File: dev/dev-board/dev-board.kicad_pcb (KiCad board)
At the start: 4 copper layers, 90 x 70 mm, 123 parts, among them J5 Conn_02x10_Odd_Even, P1 HDR-IDC-2.54-2X5P, Q1 BSS138, Q2 BSS138, Q3 BSS138, Q4 BSS138, SW1 TS342A2P, SW2 TS342A2P, SW3 TS342A2P, SW4 TS342A2P, SW5 TS342A2P, SW6 TS342A2P, SW7 TS342A2P, SW8 TS342A2P, U1 ESP32-WROVER-IE(16MB), U10 TPS2065CDBV, U11 PESD5V0U2BT, U12 PESD5V0S1BA_C5261083, U13 PCM5102APWR, U14 CH340C, U16 PESD5V0U2BT, U2 ESP32-S3-WROOM-1(N16R8), U3 CH340C, U4 TPS2065CDBV, U5 AP7361C-33E, U6 PESD5V0U2BT, U7 PESD5V0S1BA_C5261083, U8 ZX-HY2.0-4PWZ, U9 ZX-HY2.0-4PWZ

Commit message: wiring donw. checking DRC
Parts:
- moved C6 13.6 mm to (90.0, 200.8), turned to -90 degrees
- moved R10 12.2 mm to (102.0, 208.2)
- moved R3 11.5 mm to (89.8, 197.0), turned to -90 degrees
- moved TP1 11.3 mm to (100.0, 200.5)
- moved TP2 10.3 mm to (73.2, 203.5)
- moved TP4 10.1 mm to (76.8, 203.5)
- moved C12 8.38 mm to (48.5, 206.0)
- moved R37 5.27 mm to (83.0, 202.5), turned to -90 degrees
- moved Q2 3.76 mm to (56.0, 203.5)
- moved R5 3.51 mm to (89.2, 212.5)
- moved R9 3.48 mm to (89.2, 210.5)
- moved R12 3.04 mm to (48.5, 213.5)
- moved R7 2.30 mm to (104.8, 197.0), turned to 90 degrees
- moved C4 2.06 mm to (89.8, 193.5), turned to 90 degrees
- moved D3 2.05 mm to (61.2, 246.5)
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- renumbered TX1 to TP1, TX2 to TP2, RX1 to TP3, RX2 to TP4
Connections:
- J5 pad 10: /WR-IO35 -> /WR-IO36
- J5 pad 4: /WR-IO36 -> /WR-IO35
- J5 pad 6: /WR-IO39 -> /WR-IO34
- J5 pad 8: /WR-IO34 -> /WR-IO39
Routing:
- net GND: track 5.82 -> 151.0 mm, vias 3 -> 80
- net /S3-ButtonUp: track 0.00 -> 98.1 mm, vias 0 -> 4
- net /S3-IO0: track 0.00 -> 97.4 mm, vias 0 -> 4
- net /S3-ButtonCancel: track 0.00 -> 97.3 mm, vias 0 -> 4
- net /S3-ButtonDown: track 0.00 -> 93.2 mm, vias 0 -> 4
- net /S3-ButtonEnter: track 0.00 -> 84.2 mm, vias 0 -> 5
- net /S3-USB-PWSW: track 12.5 -> 89.1 mm, vias 0 -> 2
- net /S3-EN: track 0.00 -> 71.7 mm, vias 0 -> 6
- net /S3-I2C1-SDA: track 0.00 -> 67.9 mm
- net /WR-IO15: track 0.00 -> 64.6 mm, vias 0 -> 4
- net /S3-I2C1-SCL: track 0.00 -> 64.2 mm
- net /S3-ResetSub: track 0.00 -> 63.4 mm, vias 0 -> 4
- net /WR-IO12: track 0.00 -> 59.0 mm, vias 0 -> 1
- net VSYS: track 37.1 -> 95.8 mm, vias 13 -> 14
- net /WR-IO4: track 0.00 -> 58.1 mm, vias 0 -> 1
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- added copper zone on F.Cu, net GND

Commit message: checking before release
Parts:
- added G***: LOGO, LogoLibrary:logo_sym.kicad2_mod, F.Cu at (110.0, 248.0)
- moved C22 1.75 mm to (45.5, 241.5)
- moved C23 1.75 mm to (45.5, 239.8)
- renumbered SW6 to Cancel, SW8 to DOWN, SW7 to Enter, TP3 to RX1, TP4 to RX2, SW3 to S3-EN, SW1 to S3-IO0, TP1 to TX1, TP2 to TX2, SW5 to UP, SW4 to WR-EN, SW2 to WR-IO0
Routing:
- net GND: track 151.0 -> 219.7 mm, vias 80 -> 315
- net /S3-ButtonEnter: track 84.2 -> 78.9 mm
- net /S3-MTMS: track 34.8 -> 37.1 mm
- net +3V3: track 78.7 -> 80.2 mm
- net /S3-IO0: track 97.4 -> 96.7 mm
- net /WR-IO14: track 49.7 -> 50.2 mm
- net /WR-IO15: track 64.6 -> 65.1 mm
- added copper zone on B.Cu, net GND
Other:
- board text added: "Narya v3 dev R2"

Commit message: r2 candidate
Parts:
- turned C30 to 180 degrees
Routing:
- net GND: track 219.7 -> 234.5 mm, vias 315 -> 309
- net Net-(LDO1-VOUT): track 29.5 -> 22.2 mm
- net Net-(U13-CPGND): track 10.5 -> 6.14 mm
- net /S3-EN: track 71.7 -> 74.9 mm
- net /S3-ResetSub: track 63.4 -> 65.9 mm
- net /S3-ButtonDown: track 93.2 -> 95.3 mm
- net +3V3: track 80.2 -> 82.3 mm, vias 30 -> 29
- net /S3-ButtonEnter: track 78.9 -> 80.9 mm
- net Net-(U13-XSMT): track 6.15 -> 7.69 mm

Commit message: r2 candidate (fix CH340 V3-VCC)
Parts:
- renumbered S3-IO0 to SW1, WR-IO0 to SW2, S3-EN to SW3, WR-EN to SW4, UP to SW5, Cancel to SW6, Enter to SW7, DOWN to SW8
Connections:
- C4 pad 2: Net-(U3-V3) -> +3V3
- C5 pad 2: Net-(U14-V3) -> +3V3
- U14 pad 4: Net-(U14-V3) -> +3V3
- U3 pad 4: Net-(U3-V3) -> +3V3
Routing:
- net +3V3: track 82.3 -> 106.9 mm, vias 29 -> 31
- net Net-(U3-V3): track 11.9 -> 0.00 mm
- net Net-(U14-V3): track 10.4 -> 0.00 mm
- net GND: vias 309 -> 307

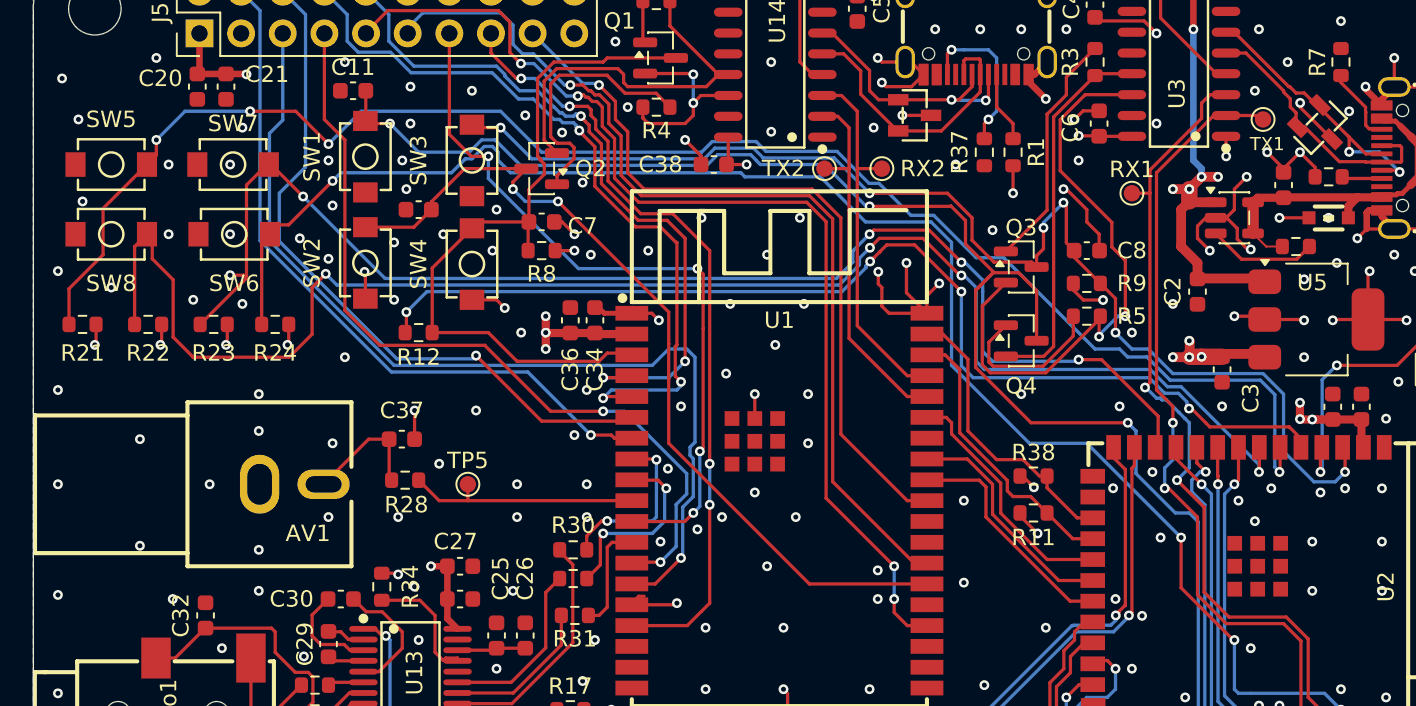
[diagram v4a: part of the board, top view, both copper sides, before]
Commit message: r2 candidate (fix silk, add via around ESP32 GND pad)
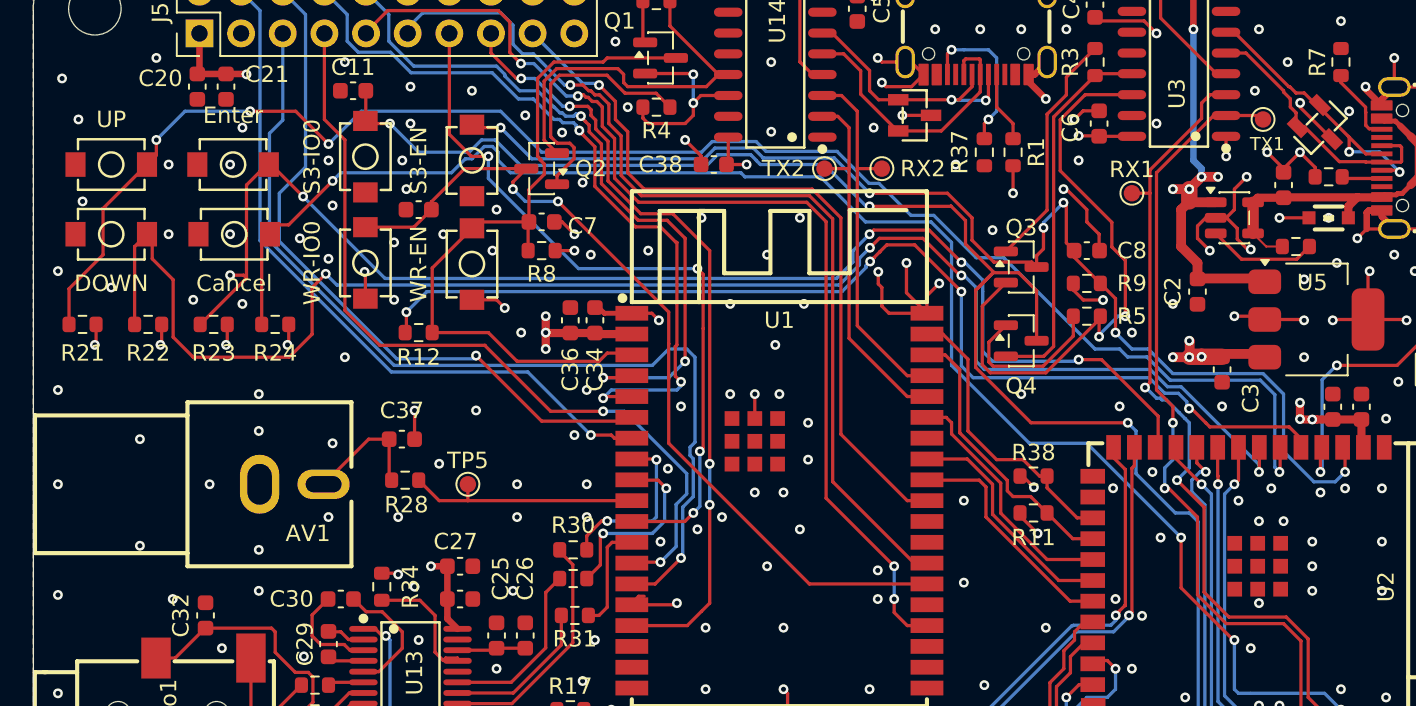
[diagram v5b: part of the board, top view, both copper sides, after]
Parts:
- renumbered SW6 to Cancel, SW8 to DOWN, SW7 to Enter, SW3 to S3-EN, SW1 to S3-IO0, SW5 to UP, SW4 to WR-EN, SW2 to WR-IO0
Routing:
- net GND: track 234.5 -> 239.7 mm, vias 307 -> 312
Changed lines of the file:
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@@
 		(layer "F.Cu")
 		(at 51.75 203 90)
-		(property "Reference" "SW3"
+		(property "Reference" "S3-EN"
 			(at 0 -3.25 90)
 			(layer "F.SilkS")
@@
 		(layer "F.Cu")
 		(at 45.25 202.77 90)
-		(property "Reference" "SW1"
+		(property "Reference" "S3-IO0"
 			(at 0 -3.25 90)
 			(layer "F.SilkS")
@@
 				(font
 					(size 1 1)
-					(thickness 0.15)
+					(thickness 0.125)
 				)
 			)
@@
 		(layer "F.Cu")
 		(at 45.25 209.25 90)
-		(property "Reference" "SW2"
+		(property "Reference" "WR-IO0"
 			(at 0 -3.25 90)
 			(layer "F.SilkS")
@@
 		(layer "F.Cu")
 		(at 37.18 203.25)
-		(property "Reference" "SW7"
-			(at 0 -2.5 0)
+		(property "Reference" "Enter"
+			(at 0 -3 0)
 			(layer "F.SilkS")
 			(effects
@@
 		(layer "F.Cu")
 		(at 37.25 207.5)
-		(property "Reference" "SW6"
+		(property "Reference" "Cancel"
 			(at 0 3 0)
 			(layer "F.SilkS")
@@
 		(layer "F.Cu")
 		(at 29.75 203.25)
-		(property "Reference" "SW5"
+		(property "Reference" "UP"
 			(at 0 -2.75 0)
 			(layer "F.SilkS")
@@
 		(layer "F.Cu")
 		(at 29.75 207.5)
-		(property "Reference" "SW8"
+		(property "Reference" "DOWN"
 			(at 0 3 0)
 			(layer "F.SilkS")
@@
 		(layer "F.Cu")
 		(at 51.75 209.32 90)
-		(property "Reference" "SW4"
+		(property "Reference" "WR-EN"
 			(at 0 -3.25 90)
 			(layer "F.SilkS")
@@
 	)
 	(via
+		(at 99.75 230)
+		(size 0.6)
+		(drill 0.3)
+		(layers "F.Cu" "B.Cu")
+		(free yes)
+		(net 3)
+	)
+	(via
 		(at 91 239.5)
 		(size 0.6)
@@
 	)
 	(via
-		(at 99.5 225)
+		(at 99.75 225)
 		(size 0.6)
 		(drill 0.3)
@@
 	)
 	(via
+		(at 101.25 225)
+		(size 0.6)
+		(drill 0.3)
+		(layers "F.Cu" "B.Cu")
+		(free yes)
+		(net 3)
+	)
+	(via
 		(at 60.5 195.75)
 		(size 0.6)
@@
 	)
 	(via
-		(at 72.25 220.25)
+		(at 72.25 221.25)
 		(size 0.6)
 		(drill 0.3)
@@
 	)
 	(via
-		(at 72.25 217.25)
+		(at 72.25 219)
 		(size 0.6)
 		(drill 0.3)
@@
 	)
 	(via
+		(at 103 227.75)
+		(size 0.6)
+		(drill 0.3)
+		(layers "F.Cu" "B.Cu")
+		(free yes)
+		(net 3)
+	)
+	(via
 		(at 81.5 254.75)
 		(size 0.6)
@@
 	)
 	(via
+		(at 70.75 223.25)
+		(size 0.6)
+		(drill 0.3)
+		(layers "F.Cu" "B.Cu")
+		(free yes)
+		(net 3)
+	)
+	(via
 		(at 107.5 218.75)
 		(size 0.6)
@@
 	)
 	(via
-		(at 71.5 224.75)
+		(at 71.75 225.5)
 		(size 0.6)
 		(drill 0.3)
@@
 	)
 	(via
+		(at 70.5 217.25)
+		(size 0.6)
+		(drill 0.3)
+		(layers "F.Cu" "B.Cu")
+		(free yes)
+		(net 3)
+	)
+	(via
 		(at 42.25 242)
 		(size 0.6)
@@
 	)
 	(via
-		(at 67.25 216)
+		(at 67.5 217.25)
 		(size 0.6)
 		(drill 0.3)
@@
 	)
 	(segment
-		(start 99.5 225)
-		(end 93.75 225)
+		(start 69 211.25)
+		(end 66.25 208.5)
 		(width 0.2)
 		(layer "In1.Cu")
@@
 	)
 	(segment
-		(start 69 217.25)
-		(end 69 212.09853)
-		(width 0.2)
-		(layer "In1.Cu")
-		(net 3)
-	)
-	(segment
 		(start 92.75 230.642209)
 		(end 92.617314 230.774895)
@@
 	)
 	(segment
+		(start 93.25 222)
+		(end 91.844321 222)
+		(width 0.2)
+		(layer "In1.Cu")
+		(net 3)
+	)
+	(segment
 		(start 92.875 225.875)
 		(end 92.75 226)
@@
 	)
 	(segment
-		(start 69 212.09853)
-		(end 65.450735 208.549265)
+		(start 55.5 249)
+		(end 57.5 249)
 		(width 0.2)
 		(layer "In1.Cu")
@@
 	)
 	(segment
-		(start 55.5 249)
-		(end 57.5 249)
+		(start 98.475737 240.324266)
+		(end 99.002471 240.851)
 		(width 0.2)
 		(layer "In1.Cu")
@@
 	)
 	(segment
-		(start 98.475737 240.324266)
-		(end 99.002471 240.851)
+		(start 66 208.5)
+		(end 65.75 208.25)
 		(width 0.2)
 		(layer "In1.Cu")
@@
 	)
 	(segment
-		(start 93.75 225)
-		(end 92.875 225.875)
-		(width 0.2)
-		(layer "In1.Cu")
-		(net 3)
-	)
-	(segment
 		(start 69 217.25)
 		(end 65.25 217.25)
@@
 	)
 	(segment
+		(start 91.844321 222)
+		(end 90.852216 222.992105)
+		(width 0.2)
+		(layer "In1.Cu")
+		(net 3)
+	)
+	(segment
+		(start 93.75 225)
+		(end 92.875 225.875)
+		(width 0.2)
+		(layer "In1.Cu")
+		(net 3)
+	)
+	(segment
 		(start 57.5 249)
 		(end 58.5 250)
@@
 	)
 	(segment
+		(start 66.25 208.5)
+		(end 66 208.5)
+		(width 0.2)
+		(layer "In1.Cu")
+		(net 3)
+	)
+	(segment
+		(start 69 217.25)
+		(end 69 211.25)
+		(width 0.2)
+		(layer "In1.Cu")
+		(net 3)
+	)
+	(segment
 		(start 58 217.75)
 		(end 58.75 217)
@@
 	)
 	(segment
+		(start 65.75 208.25)
+		(end 65.75 206.5)
+		(width 0.2)
+		(layer "In1.Cu")
+		(net 3)
+	)
+	(segment
 		(start 64.201 222.29953)
 		(end 63.700735 221.799265)
@@
 	)
 	(segment
+		(start 99.75 225)
+		(end 93.75 225)
+		(width 0.2)
+		(layer "In1.Cu")
+		(net 3)
+	)
+	(segment
 		(start 102.25 240)
 		(end 102.75 240)
@@
 		(polygon
 			(pts
-				(xy 34.25 250) (xy 58 250) (xy 64.5 241) (xy 73.75 241) (xy 73.75 220) (xy 94.75 207.75) (xy 98 205.75)
-				(xy 98 203.75) (xy 97 203) (xy 59.75 219.25) (xy 59.75 234.25) (xy 49.75 240.75) (xy 34.25 240.75)
+				(xy 34.25 250) (xy 58 250) (xy 64.5 241) (xy 74.5 241) (xy 79.25 217.5) (xy 95.75 206.5) (xy 98 205.75)
+				(xy 98 203.75) (xy 97 203) (xy 59.75 219.25) (xy 59.75 234.25) (xy 49.75 240.75) (xy 35 240.75)
 			)
 		)

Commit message: update for v3r3
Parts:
- removed RX1, RX2, TX1, TX2: TestPoint, TestPoint:TestPoint_Pad_D1.0mm
- added C17: 0.1uF, Capacitor_SMD:C_0603_1608Metric, F.Cu at (8.27, 54.0)
- added C39: 0.1uF, Capacitor_SMD:C_0603_1608Metric, F.Cu at (8.27, 55.5)
- added ERR1: LED RED, LED_SMD:LED_0805_2012Metric, F.Cu at (83.5, 60.0)
- added J1: Conn_01x03_Pin, Connector_PinHeader_2.54mm:PinHeader_1x03_P2.54mm_Vertical, F.Cu at (21.5, 58.7)
- added J2: Conn_01x02_Socket, Connector_PinSocket_2.54mm:PinSocket_1x02_P2.54mm_Vertical, F.Cu at (4.77, 52.3)
- added R39: 0, Resistor_SMD:R_0603_1608Metric, F.Cu at (80.3, 53.5)
- added R40: 0, Resistor_SMD:R_0603_1608Metric, F.Cu at (5.02, 55.8)
- added R41: 0, Resistor_SMD:R_0603_1608Metric, F.Cu at (11.3, 54.5)
- added R42: 0, Resistor_SMD:R_0603_1608Metric, F.Cu at (23.5, 23.5)
- added SW9: GT-TC018A-H0375-L1, easyeda2kicad:SW-SMD_L4.7-W3.5-P3.35-EH, F.Cu at (87.5, 57.8)
- added TP1: TestPoint, TestPoint:TestPoint_Pad_D1.0mm, F.Cu at (2.77, 58.8)
- added U15: RX8900CE_UB0, easyeda2kicad:SMD-10_L3.2-W2.5-BL_EPSON_RX8900CE, F.Cu at (6.77, 58.5)
- R12: value 100 -> 10K
- R15: value 10K -> 0
- R16: value 10K -> 2K
- moved G*** 209.9 mm to (59.5, 44.2)
- moved R16 197.4 mm to (83.5, 53.0), turned to 0 degrees
- moved C31 195.1 mm to (14.8, 48.5)
- moved Audio1 194.1 mm to (9.02, 44.2)
- moved C32 194.1 mm to (10.5, 38.2)
- moved REF4 193.6 mm to (84.8, 64.5)
- moved AV1 193.4 mm to (15.8, 31.0)
- moved REF2 193.2 mm to (5.52, 64.5)
- moved C1 191.6 mm to (76.3, 14.5)
- moved C10 191.6 mm to (12.3, 59.2)
- moved C11 191.6 mm to (19.5, 8.75)
- moved C12 191.6 mm to (23.5, 16.0)
- moved C13 191.6 mm to (26.5, 59.2)
- moved C14 191.6 mm to (34.0, 51.2)
- moved C15 191.6 mm to (43.8, 49.0)
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- renumbered Cancel to CANCEL, P1 to JTAG, REF** to REF1, REF** to REF2, REF** to REF3, REF** to REF4, D1 to STAT1
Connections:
- C13 pad 2: VSYS -> Net-(J1-Pin_2)
- R12 pad 1: /S3-ResetSub -> +3V3
- R12 pad 2: /WR-EN -> Net-(U15-~{INT})
- R15 pad 1: /S3-I2C2-SDA -> Net-(U15-~{INT})
- R15 pad 2: +3V3 -> /S3-MTDO
- R16 pad 1: /S3-I2C2-SCL -> Net-(D4-A)
- R16 pad 2: +3V3 -> Net-(R16-Pad2)
- U9 pad 2: VSYS -> Net-(J1-Pin_2)
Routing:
- net Net-(U15-~{INT}): track 0.00 -> 53.8 mm, vias 0 -> 2
- net /S3-EN: track 74.9 -> 104.8 mm, vias 6 -> 7
- net /S3-MTCK: track 24.7 -> 50.4 mm, vias 2 -> 3
- net /S3-I2C1-SCL: track 64.2 -> 84.8 mm
- net /S3-I2C1-SDA: track 67.9 -> 84.8 mm, vias 0 -> 1
- net /S3-StatLED1: track 15.2 -> 26.8 mm, vias 2 -> 0
- net /WR-NTSC: track 14.5 -> 5.13 mm
- net Net-(J1-Pin_2): track 0.00 -> 9.08 mm
- net Net-(D4-A): track 0.00 -> 8.48 mm
- net Net-(J2-Pin_1): track 0.00 -> 8.06 mm
- net Net-(AV1-Pad2): track 7.70 -> 15.1 mm
- net Net-(R16-Pad2): track 0.00 -> 5.50 mm, vias 0 -> 2
- net Net-(D1-A): track 2.30 -> 7.04 mm
- net /S3-I2C2-SDA: track 56.8 -> 52.4 mm, vias 2 -> 1
- net Net-(U15-FOUT): track 0.00 -> 4.15 mm, vias 0 -> 2
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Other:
- board text added: "- +"
- board text added: "3.3V"
- board text added: "5V"
- board text added: "ERR"
- board text added: "Narya v3 dev R3"
- board text added: "RESET"
- board text added: "STAT"
- board text removed: "Narya v3 dev R2"
